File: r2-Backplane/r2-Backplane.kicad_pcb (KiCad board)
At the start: 4 copper layers, 24.8 x 67.1 mm, 48 parts, among them CON1 USB-MICRO-B, P1 CONN_01X01, P2 CONN_01X02, P3 CONN_02X16, P4 HiRose-02X15, P6 DEBUG, U1 LSF0204x, U2 LSF0204x, U3 LSF0204x, U4 LSF0204x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

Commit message: BOM filled out, but board not verified.
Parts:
- removed R2, R5, R6: 1k, Resistors_SMD:R_0402_NoSilk
- added RP2: 10k, r2Parts:RES_4_EXBN8V, F.Cu at (38.0, 58.4)
- F1: value F_Small -> 1A; footprint Resistors_SMD:R_0603_HandSoldering -> Resistors_SMD:R_0805_HandSoldering
- L1, L2: footprint iansModules:L-SMD -> r2Parts:L-SMD
- R3: value 470 -> 1k
- U5: value LTC2942 -> LTC2942-1
- moved F1 0.18 mm to (45.1, 83.3), turned to 180 degrees
- turned R3 to 270 degrees
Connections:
- F1 pad 1: /Vlipo -> Net-(F1-Pad1)
- F1 pad 2: Net-(F1-Pad2) -> /Vlipo
- P2 pad 2: Net-(F1-Pad2) -> Net-(F1-Pad1)
- P3 pad N0: GND -> (no net)
- P3 pad N1: GND -> (no net)
- R3 pad 1: /VCCUSB -> Net-(D1-Pad2)
- R3 pad 2: Net-(D1-Pad2) -> /VCCUSB
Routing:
- net Net-(F1-Pad1): track 0.00 -> 3.98 mm
- net Net-(F1-Pad2): track 3.92 -> 0.00 mm
- net /VCC1: track 43.1 -> 40.7 mm
- added copper zone on F.Cu, net Net-(F1-Pad1)
- removed copper zone on F.Cu, net Net-(F1-Pad2)

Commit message: Adding small tools catch-all project.
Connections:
- RP1 pad 3: Net-(RP1-Pad3) -> GND
- RP1 pad 4: Net-(RP1-Pad4) -> GND
- RP1 pad 5: Net-(RP1-Pad5) -> GND
- RP1 pad 6: Net-(RP1-Pad6) -> GND
- U8 pad A2: Net-(U8-PadA2) -> GND
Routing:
- net /ALERT: track 11.0 -> 11.9 mm, vias 0 -> 2

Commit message: Fixed some bugs in the Dev Harness.
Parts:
- P1: moved to B.Cu
- moved P1 8.02 mm to (52.0, 45.5), turned to 325 degrees
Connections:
- P3 pad N0: (no net) -> GND
- P3 pad N1: (no net) -> GND
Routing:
- net GND: track 70.0 -> 78.4 mm, vias 17 -> 23
- net /VCC1: track 40.7 -> 45.5 mm
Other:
- board text added: "Digitabulum Backplane 2017-11-10"
- board text removed: "Digitabulum Backplane 2017-06-06"

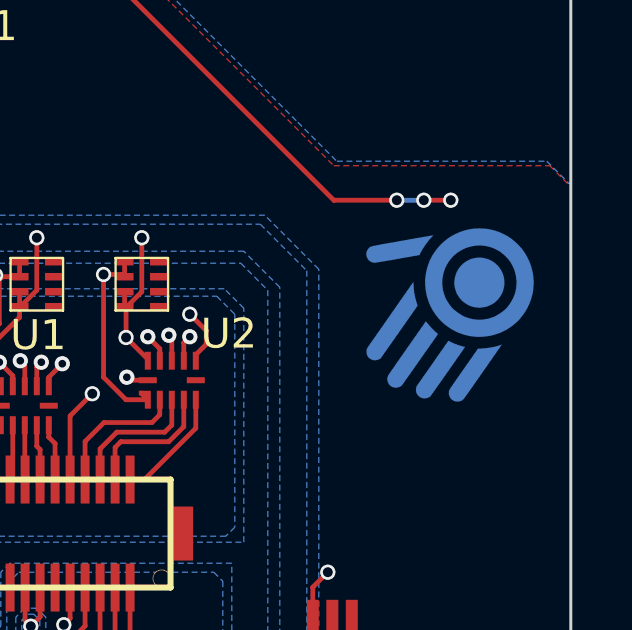
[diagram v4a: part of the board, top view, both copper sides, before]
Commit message: Updating to r2 backplane fixes from last year.
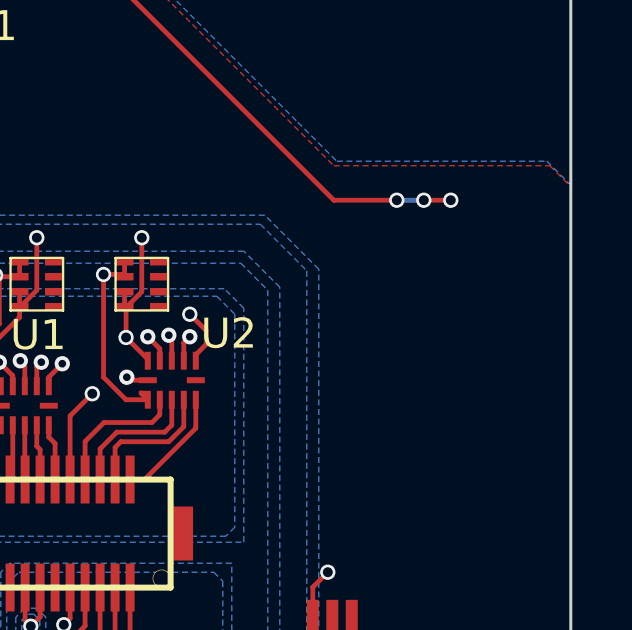
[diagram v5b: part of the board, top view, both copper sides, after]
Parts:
- added P1: CONN_01X01, r2Parts:ManuvrLogo, B.Cu at (53.3, 51.8)
- P1: footprint manuvr_logo:ManuvrLogo -> r2Parts:ManuvrLogo; moved to F.Cu
- moved P1 1.52 mm to (53.3, 46.2), turned to 135 degrees
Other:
- net class Default: clearance 0.16 -> 0.13; via_dia 0.51 -> 0.4; via_drill 0.33 -> 0.28
- net class GND: clearance 0.16 -> 0.13
- net class High-Current: clearance 0.16 -> 0.13
- net class VCC: clearance 0.16 -> 0.13
- rule trace_clearance: 0.16 -> 0.13
- rule via_min_drill: 0.21 -> 0.26
- rule via_min_size: 0.33 -> 0.381

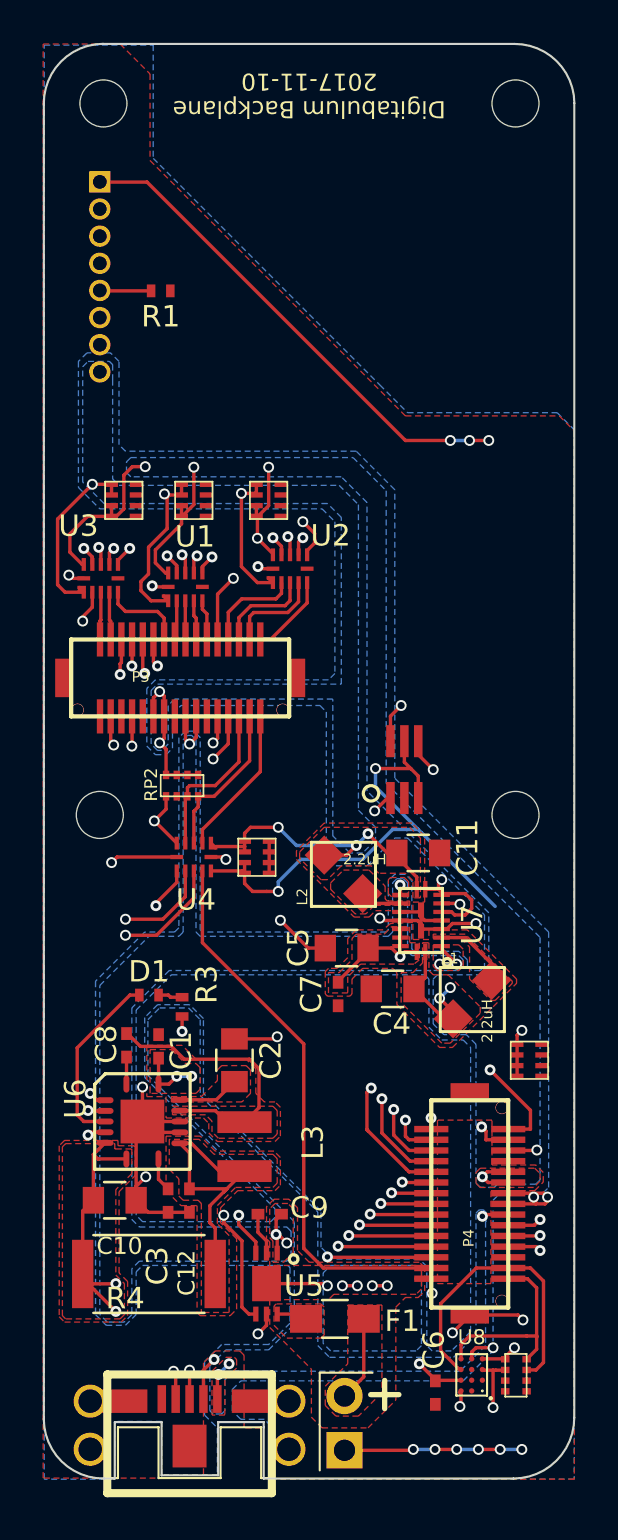
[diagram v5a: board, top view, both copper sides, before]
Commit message: Compute module will now take either WROOM32 module.
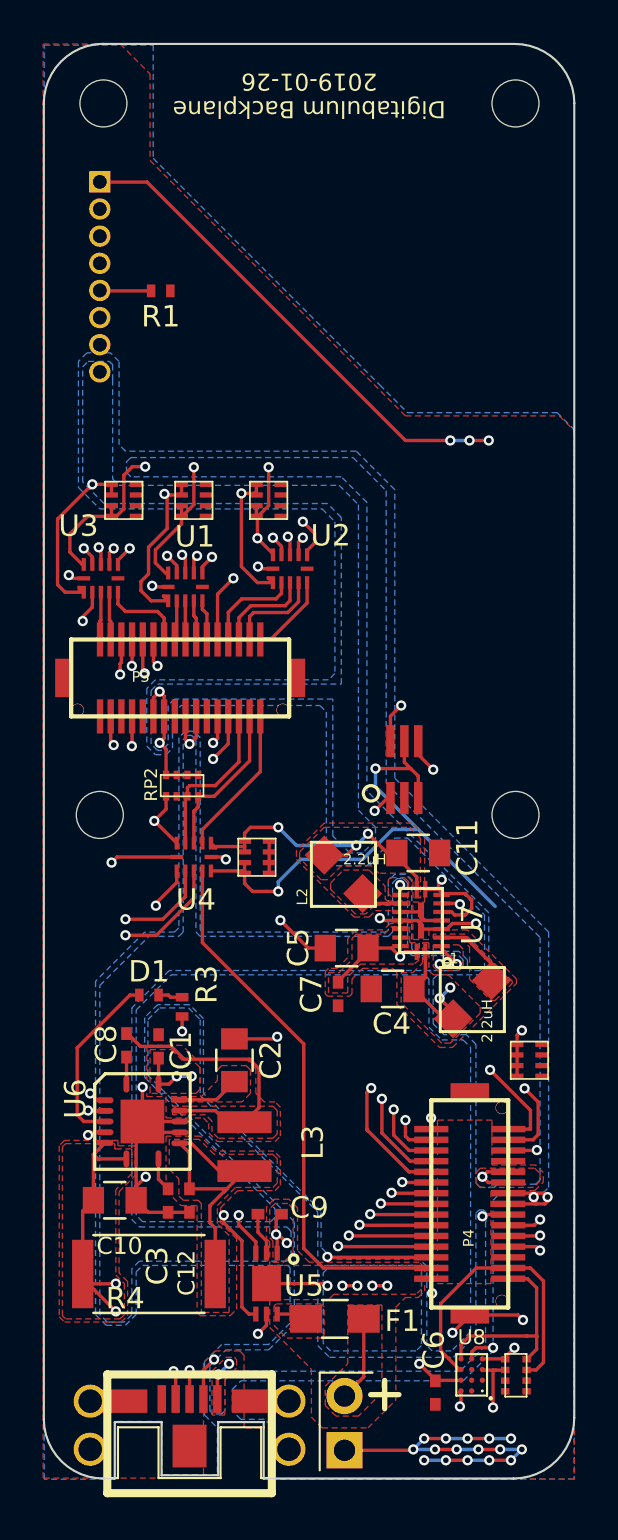
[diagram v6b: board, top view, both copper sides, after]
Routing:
- net GND: track 78.4 -> 88.0 mm, vias 23 -> 33
- net /PIN_0: track 51.2 -> 54.9 mm
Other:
- net class Default: via_dia 0.4 -> 0.48; via_drill 0.28 -> 0.26
- net class GND removed
- net class High-Current removed
- net class VCC removed
- board text added: "Digitabulum Backplane 2019-01-26"
- board text removed: "Digitabulum Backplane 2017-11-10"
